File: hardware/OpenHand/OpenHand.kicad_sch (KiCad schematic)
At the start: 98 parts, among them J1 CONN_MOTOR_1, J10 CONN_JTAG, J11 CONN_FDBK_2, J12 CONN_EMG_2, J13 CONN_POS_3, J2 CONN_MOTOR_2, J3 CONN_BATT, J4 USB_C_CONN, J5 CONN_POS_1, J6 CONN_MOTOR_3, J7 CONN_FDBK_1, J8 CONN_EMG_1, J9 CONN_POS_2, Q1 2N7002, Q2 2N7002, SW1 SW_Push, SW2 BTN_RST, SW3 BTN_BOOT, U1 CH340C, U2 STM32F103RETx

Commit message: update schm and pcb again
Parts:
- removed JP9: JMPR_RST, Jumper:SolderJumper-2_P1.3mm_Bridged_RoundedPad1.0x1.5mm, symbol Jumper:SolderJumper_2_Bridged
- removed JP9: JMPR_BOOT, Jumper:SolderJumper-2_P1.3mm_Bridged_RoundedPad1.0x1.5mm, symbol Jumper:SolderJumper_2_Bridged
- removed TP50: TP_UC_BOOT, TestPoint:TestPoint_Pad_D1.0mm, symbol Connector:TestPoint_Small
- removed TP50: TP_UC_RST, TestPoint:TestPoint_Pad_D1.0mm, symbol Connector:TestPoint_Small
- added JP9: JMPR_RST, Jumper:SolderJumper-2_P1.3mm_Bridged_RoundedPad1.0x1.5mm, symbol Jumper:SolderJumper_2_Bridged
- added JP9: JMPR_BOOT, Jumper:SolderJumper-2_P1.3mm_Bridged_RoundedPad1.0x1.5mm, symbol Jumper:SolderJumper_2_Bridged
- added TP50: TP_UC_BOOT, TestPoint:TestPoint_Pad_D1.0mm, symbol Connector:TestPoint_Small
- added TP50: TP_UC_RST, TestPoint:TestPoint_Pad_D1.0mm, symbol Connector:TestPoint_Small
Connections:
- net UC_BOOT: now also C4.1, JP9.2 (B), TP50.1
- net UC_RST: now also C3.1, JP9.2 (B), TP50.1
- net at Q1.3 (D): now also JP9.1 (A); no longer C3.1
- net at Q2.3 (D): now also JP9.1 (A); no longer C4.1
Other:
- added sheet ESP32 (ESP32.kicad_sch)
- note added: "For now we have a parallel connection to this STM32, as well as ESP32 on another sheet, so we can later select which processor we will use, and can have two prototypes: one with ESP32 and one with STM32 MCU."

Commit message: Major updates to schm and pcb, a bit better design
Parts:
- removed J4: USB_C_CONN, Connector_USB:USB_C_Receptacle_G-Switch_GT-USB-7010ASV, symbol Connector:USB_C_Receptacle
- removed JP15, JP16, JP17, JP18: SolderJumper_2_Open, Jumper:SolderJumper-2_P1.3mm_Open_RoundedPad1.0x1.5mm, symbol Jumper:SolderJumper_2_Open
- removed JP9: JMPR_BTN_BOOT, Jumper:SolderJumper-2_P1.3mm_Bridged_RoundedPad1.0x1.5mm, symbol Jumper:SolderJumper_2_Bridged
- removed JP9: JMPR_BTN_RST, Jumper:SolderJumper-2_P1.3mm_Bridged_RoundedPad1.0x1.5mm, symbol Jumper:SolderJumper_2_Bridged
- removed JP9: JMPR_USB_P, Jumper:SolderJumper-2_P1.3mm_Bridged_RoundedPad1.0x1.5mm, symbol Jumper:SolderJumper_2_Bridged
- removed JP9: JMPR_RST, Jumper:SolderJumper-2_P1.3mm_Bridged_RoundedPad1.0x1.5mm, symbol Jumper:SolderJumper_2_Bridged
- removed JP9: JMPR_BOOT, Jumper:SolderJumper-2_P1.3mm_Bridged_RoundedPad1.0x1.5mm, symbol Jumper:SolderJumper_2_Bridged
- removed JP9: JMPR_TX, Jumper:SolderJumper-2_P1.3mm_Bridged_RoundedPad1.0x1.5mm, symbol Jumper:SolderJumper_2_Bridged
- removed JP9: JMPR_USB_N, Jumper:SolderJumper-2_P1.3mm_Bridged_RoundedPad1.0x1.5mm, symbol Jumper:SolderJumper_2_Bridged
- removed JP9: JMPR_RX, Jumper:SolderJumper-2_P1.3mm_Bridged_RoundedPad1.0x1.5mm, symbol Jumper:SolderJumper_2_Bridged
- removed Q1, Q2: 2N7002, Package_TO_SOT_SMD:SOT-23, symbol Transistor_FET:2N7002
- removed R10, R7, R8, R9: 10k, Resistor_SMD:R_0805_2012Metric_Pad1.20x1.40mm_HandSolder, symbol Device:R
- removed R4: 1k, Resistor_SMD:R_0805_2012Metric_Pad1.20x1.40mm_HandSolder, symbol Device:R
- removed SW3: BTN_BOOT, Button_Switch_SMD:SW_Tactile_SPST_NO_Straight_CK_PTS636Sx25SMTRLFS, symbol Switch:SW_Push
- removed TP50: TP_UC_PIN_PC15, TestPoint:TestPoint_Pad_D1.0mm, symbol Connector:TestPoint_Small
- removed TP50: TP_UC_BOOT, TestPoint:TestPoint_Pad_D1.0mm, symbol Connector:TestPoint_Small
- removed TP50: TP_UC_PIN_PC0, TestPoint:TestPoint_Pad_D1.0mm, symbol Connector:TestPoint_Small
- removed TP50: TP_UC_PIN_PC14, TestPoint:TestPoint_Pad_D1.0mm, symbol Connector:TestPoint_Small
- removed TP50: TP_USB_D_P, TestPoint:TestPoint_Pad_D1.0mm, symbol Connector:TestPoint_Small
- removed TP50: TP_HW_REV_1, TestPoint:TestPoint_Pad_D1.0mm, symbol Connector:TestPoint_Small
- removed TP50: TP_UC_PIN_PC3, TestPoint:TestPoint_Pad_D1.0mm, symbol Connector:TestPoint_Small
- removed TP50: TP_UC_PIN_PD2, TestPoint:TestPoint_Pad_D1.0mm, symbol Connector:TestPoint_Small
- removed TP50: TP_UC_SCL, TestPoint:TestPoint_Pad_D1.0mm, symbol Connector:TestPoint_Small
- removed TP50: TP_HW_REV_2, TestPoint:TestPoint_Pad_D1.0mm, symbol Connector:TestPoint_Small
- removed TP50: TP_UC_PIN_PB10, TestPoint:TestPoint_Pad_D1.0mm, symbol Connector:TestPoint_Small
- removed TP50: TP_UC_PIN_PD0, TestPoint:TestPoint_Pad_D1.0mm, symbol Connector:TestPoint_Small
- removed TP50: TP_UC_SDA, TestPoint:TestPoint_Pad_D1.0mm, symbol Connector:TestPoint_Small
- removed TP50: TP_UC_PIN_PB11, TestPoint:TestPoint_Pad_D1.0mm, symbol Connector:TestPoint_Small
- removed TP50: TP_LED_2, TestPoint:TestPoint_Pad_D1.0mm, symbol Connector:TestPoint_Small
- removed TP50: TP_UC_RST, TestPoint:TestPoint_Pad_D1.0mm, symbol Connector:TestPoint_Small
- removed TP50: TP_UC_PIN_PC13, TestPoint:TestPoint_Pad_D1.0mm, symbol Connector:TestPoint_Small
- removed TP50: TP_UC_PIN_PD1, TestPoint:TestPoint_Pad_D1.0mm, symbol Connector:TestPoint_Small
- removed TP50: TP_UC_PIN_PC1, TestPoint:TestPoint_Pad_D1.0mm, symbol Connector:TestPoint_Small
- removed TP50: TP_LED_1, TestPoint:TestPoint_Pad_D1.0mm, symbol Connector:TestPoint_Small
- removed TP50: TP_UC_PIN_PC2, TestPoint:TestPoint_Pad_D1.0mm, symbol Connector:TestPoint_Small
- removed TP50: TP_HW_REV_3, TestPoint:TestPoint_Pad_D1.0mm, symbol Connector:TestPoint_Small
- removed TP50: TP_UC_PIN_PB2, TestPoint:TestPoint_Pad_D1.0mm, symbol Connector:TestPoint_Small
- removed TP50: TP_HW_REV_4, TestPoint:TestPoint_Pad_D1.0mm, symbol Connector:TestPoint_Small
- removed U1: CH340C, Package_SO:SOIC-16_3.9x9.9mm_P1.27mm, symbol Interface_USB:CH340C
- added C5, C6: 100n, Capacitor_SMD:C_0805_2012Metric, symbol Device:C
- added J5: USB_C_CONN, Connector_USB:USB_C_Receptacle_G-Switch_GT-USB-7010ASV, symbol Connector:USB_C_Receptacle_USB2.0
- added JP14, JP7, JP8, JP9: SolderJumper_2_Open, Jumper:SolderJumper-2_P1.3mm_Open_RoundedPad1.0x1.5mm, symbol Jumper:SolderJumper_2_Open
- added R13, R16, R5, R55: 10k, Resistor_SMD:R_0805_2012Metric, symbol Device:R
- added R52: 1.5k, Resistor_SMD:R_0805_2012Metric, symbol Device:R
- added R54: 47k, Resistor_SMD:R_0805_2012Metric, symbol Device:R
- added SW1: BTN_RST, Button_Switch_SMD:SW_Tactile_SPST_NO_Straight_CK_PTS636Sx25SMTRLFS, symbol Switch:SW_Push
- added TP50: TP_UC_PIN_PD2, TestPoint:TestPoint_Pad_D1.0mm, symbol Connector:TestPoint_Small
- added TP50: TP_BATT_SENSE, TestPoint:TestPoint_Pad_D1.0mm, symbol Connector:TestPoint_Small
- added TP50: TP_UC_PIN_PC12, TestPoint:TestPoint_Pad_D1.0mm, symbol Connector:TestPoint_Small
- added TP50: TP_HALL_03, TestPoint:TestPoint_Pad_D1.0mm, symbol Connector:TestPoint_Small
- added TP50: TP_UC_SCL, TestPoint:TestPoint_Pad_D1.0mm, symbol Connector:TestPoint_Small
- added TP50: TP_UC_SDA, TestPoint:TestPoint_Pad_D1.0mm, symbol Connector:TestPoint_Small
- added TP50: TP_BTN_RST, TestPoint:TestPoint_Pad_D1.0mm, symbol Connector:TestPoint_Small
- added TP50: TP_BTN_BOOT, TestPoint:TestPoint_Pad_D1.0mm, symbol Connector:TestPoint_Small
- added TP50: TP_USB_D_P, TestPoint:TestPoint_Pad_D1.0mm, symbol Connector:TestPoint_Small
- added TP50: TP_UC_PIN_PA6, TestPoint:TestPoint_Pad_D1.0mm, symbol Connector:TestPoint_Small
- added TP50: TP_UC_PIN_PA5, TestPoint:TestPoint_Pad_D1.0mm, symbol Connector:TestPoint_Small
- added TP50: TP_HALL_01, TestPoint:TestPoint_Pad_D1.0mm, symbol Connector:TestPoint_Small
- added TP50: TP_UC_PIN_PD1, TestPoint:TestPoint_Pad_D1.0mm, symbol Connector:TestPoint_Small
- added TP50: TP_HALL_02, TestPoint:TestPoint_Pad_D1.0mm, symbol Connector:TestPoint_Small
- C1: value 1u -> 100n; footprint Capacitor_SMD:C_1206_3216Metric_Pad1.33x1.80mm_HandSolder -> Capacitor_SMD:C_0805_2012Metric
- C2, C3, C4: footprint Capacitor_SMD:C_1206_3216Metric_Pad1.33x1.80mm_HandSolder -> Capacitor_SMD:C_0805_2012Metric
- D1, D2: footprint LED_SMD:LED_0805_2012Metric -> LED_SMD:LED_1210_3225Metric
- R1: value 5k1 -> 10k; footprint Resistor_SMD:R_0805_2012Metric_Pad1.20x1.40mm_HandSolder -> Resistor_SMD:R_0805_2012Metric
- R10: renamed from R13; footprint Resistor_SMD:R_0805_2012Metric_Pad1.20x1.40mm_HandSolder -> Resistor_SMD:R_0805_2012Metric
- R14, R15, R2, R51, R52: footprint Resistor_SMD:R_0805_2012Metric_Pad1.20x1.40mm_HandSolder -> Resistor_SMD:R_0805_2012Metric
- R3: value 1k -> 5k1; footprint Resistor_SMD:R_0805_2012Metric_Pad1.20x1.40mm_HandSolder -> Resistor_SMD:R_0805_2012Metric
- R8: renamed from R12; footprint Resistor_SMD:R_0805_2012Metric_Pad1.20x1.40mm_HandSolder -> Resistor_SMD:R_0805_2012Metric
- R9: renamed from R11; footprint Resistor_SMD:R_0805_2012Metric_Pad1.20x1.40mm_HandSolder -> Resistor_SMD:R_0805_2012Metric
- SW2: value BTN_RST -> BTN_BOOT
- TP50: value TP_UC_PIN_PB5 -> TP_UC_PIN_PB12
- renumbered J5 to J4, RV2 to RV1, RV3 to RV2, RV1 to RV3, SW1 to SW3, U2 to U1
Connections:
- net MOTOR_1_EN is gone; now on an unnamed net: U1.33 (PB12)
- net MOTOR_3_UC2 is gone; now on net UC_TX: U1.51 (PC10)
- net TRIM_POT_1 is gone; now on net TRIM_POT_01: JP9.2 (B)
- net TRIM_POT_2 is gone; now on net TRIM_POT_02: JP9.2 (B)
- net TRIM_POT_3 is gone; now on net TRIM_POT_03: JP9.2 (B)
- net USB_D_N is gone; now on net USB_D-: TP34.1
- net +3V3: now also C3.1, C4.1, R1.1, C5.1, C6.1, R13.1, R16.1, R5.1, R52.2
- net +5V: now also J5.A4 (VBUS), J5.A9 (VBUS), J5.B4 (VBUS), J5.B9 (VBUS); no longer C1.1
- net Earth: now also JP11.1 (A), JP12.1 (A), JP13.1 (A), R3.2, C5.2, C6.2, J5.A1 (GND), J5.A12 (GND), J5.B1 (GND), J5.B12 (GND), JP14.1 (A), R55.1, SW1.2; no longer R1.2
- net HALL_SENS_01_S: now also U1.9 (PC1), TP50.1
- net HALL_SENS_02_S: now also U1.10 (PC2), TP50.1
- net HALL_SENS_03_S: now also U1.11 (PC3), TP50.1
- net LED_1: now also U1.57 (PB5); no longer U1.52 (PC11)
- net LED_2: now also U1.58 (PB6); no longer U1.53 (PC12)
- net UC_BOOT: now also C2.1, SW2.1, R5.2, TP50.1; no longer C4.1
- net UC_RST: now also C1.1, R1.2, SW1.1, TP50.1; no longer C3.1
- net UC_RX: now also U1.52 (PC11); no longer U1.59 (PB7)
- net UC_SCL: now also TP50.1
- net UC_SDA: now also TP50.1
- net UC_TX: no longer U1.58 (PB6)
- net HW_REV_03: now reaches U1.4 (PC15)
- net HW_REV_03: now also JP13.2 (B), JP9.1 (A)
- net at R15.2: now also JP9.2 (B)
- net HW_REV_01: now reaches JP11.2 (B)
- net HW_REV_01: now also U1.2 (PC13), JP7.1 (A)
- net at JP10.2 (B): now also R16.2
- net at U1.8 (PC0): now also R54.1, R55.2, TP50.1
- net at R14.2: now also JP8.2 (B); no longer SW2.1
- net at R2.1: now also J5.A5 (CC1)
- net HW_REV_02: now reaches U1.3 (PC14)
- net HW_REV_02: now also JP12.2 (B), JP8.1 (A)
- net at R3.1: now also J5.B5 (CC2)
- net at U1.54 (PD2): now also TP50.1
- net at TP50.1: no longer U1.57 (PB5)
- net MOTOR_03_FAULT: now reaches U1.29 (PB10)
- net HW_REV_04: now reaches U1.5 (PD0)
- net HW_REV_04: now also JP10.1 (A), JP14.2 (B)
- net HAPTIC_FAULT: now reaches U1.30 (PB11)
- net MOTOR_02_FAULT: now reaches U1.28 (PB2)
- net at U1.6 (PD1): now also TP50.1
- net ADC_1_ALERT_RDY renamed MOTOR_02_EN
- net ADC_2_ALERT_RDY renamed MOTOR_03_EN
- net BTN_1 renamed BTN_01
- net BTN_01: now also U1.59 (PB7)
- net EMG_1_N renamed EMG_01_P
- net EMG_1_P renamed EMG_01_N
- net EMG_1_UC renamed HAPTIC_EN
- net EMG_2_N renamed EMG_02_P
- net EMG_2_P renamed EMG_02_N
- net EMG_2_UC renamed MOTOR_01_FAULT
- net FDBK_MOTOR_1_N renamed HAPTIC_01_N
- net FDBK_MOTOR_1_P renamed HAPTIC_01_P
- net FDBK_MOTOR_1_UC1 renamed HAPTIC_01_PWM
- net FDBK_MOTOR_1_UC2 renamed MOTOR_03_PWM
- net FDBK_MOTOR_2_N renamed HAPTIC_02_N
- net FDBK_MOTOR_2_P renamed HAPTIC_02_P
- net FDBK_MOTOR_2_UC1 renamed MOTOR_03_DIR
- net FDBK_MOTOR_2_UC2 renamed MOTOR_02_DIR
- net FDBK_MOTOR_EN renamed HAPTIC_01_DIR
- net FDBK_MOTOR_FAULT renamed MOTOR_01_EN
- net HW_REV_1 renamed TRIM_POT_01
- net TRIM_POT_01: no longer JP10.1 (A)
- net HW_REV_2 renamed TRIM_POT_02
- net TRIM_POT_02: no longer JP11.1 (A)
- net HW_REV_3 renamed TRIM_POT_03
- net TRIM_POT_03: no longer JP12.1 (A)
- net HW_REV_4 renamed EMG_01_UC
- net EMG_01_UC: no longer JP13.1 (A)
- net MOTOR_1_FAULT renamed EMG_02_UC
- net MOTOR_1_N renamed MOTOR_01_N
- net MOTOR_1_P renamed MOTOR_01_P
- net MOTOR_1_UC1 renamed MOTOR_02_PWM
- net MOTOR_1_UC2 renamed USB_D-
- net USB_D-: now also J5.A6 (D+), J5.B6 (D+)
- net MOTOR_2_EN renamed HAPTIC_02_DIR
- net MOTOR_2_FAULT: no longer names the net of U1.21 (PA5)
- net MOTOR_2_FAULT: now also TP50.1
- net MOTOR_2_N renamed MOTOR_02_N
- net MOTOR_2_P renamed MOTOR_02_P
- net MOTOR_2_UC1 renamed MOTOR_01_DIR
- net MOTOR_2_UC2 renamed USB_D+
- net USB_D+: now also J5.A7 (D-), J5.B7 (D-), R52.1, TP50.1
- net MOTOR_3_EN renamed HAPTIC_02_PWM
- net MOTOR_3_FAULT: no longer names the net of U1.22 (PA6)
- net MOTOR_3_FAULT: now also TP50.1
- net MOTOR_3_N renamed MOTOR_03_N
- net MOTOR_3_P renamed MOTOR_03_P
- net MOTOR_3_UC1 renamed MOTOR_01_PWM
- new net: TP50.1, U1.53 (PC12)
- new net: JP7.2 (B), R13.2
- new net +BATT: R54.2
- no-connect marks 15 -> 3
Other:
- sheet Control, Analog renamed Motor Control
- removed sheet ESP32
- sheet Motor Control: file Control.kicad_sch -> MotorControl.kicad_sch
- note added: "ADC inputs"
- note added: "Battery voltage sense divider: - max bat voltage ~12.6V - gives us ~2.2V on output"
- note added: "Buttons for RST and BOOT"
- note added: "Direct USB device connection"
- note added: "EMG ADC inputs"
- note added: "HW REV"
- note added: "I2C pullups"
- note added: "JTAG debugging"
- note added: "Just in case I2C"
- note added: "Just in case UART"
- note added: "STM32 decoupling caps"
- note removed: "For now we have a parallel connection to this STM32, as well as ESP32 on another sheet, so we can later select which processor we will use, and can have two prototypes: one with ESP32 and one with STM32 MCU."
- note removed: "I2C pullups and test points"
- note removed: "UART test points"
- note removed: "USB to UART converter for debugging"
- moved on the sheet: D1, D2, JP9, R10, R51, R52, R8, R9, RV1, RV2, RV3, SW3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

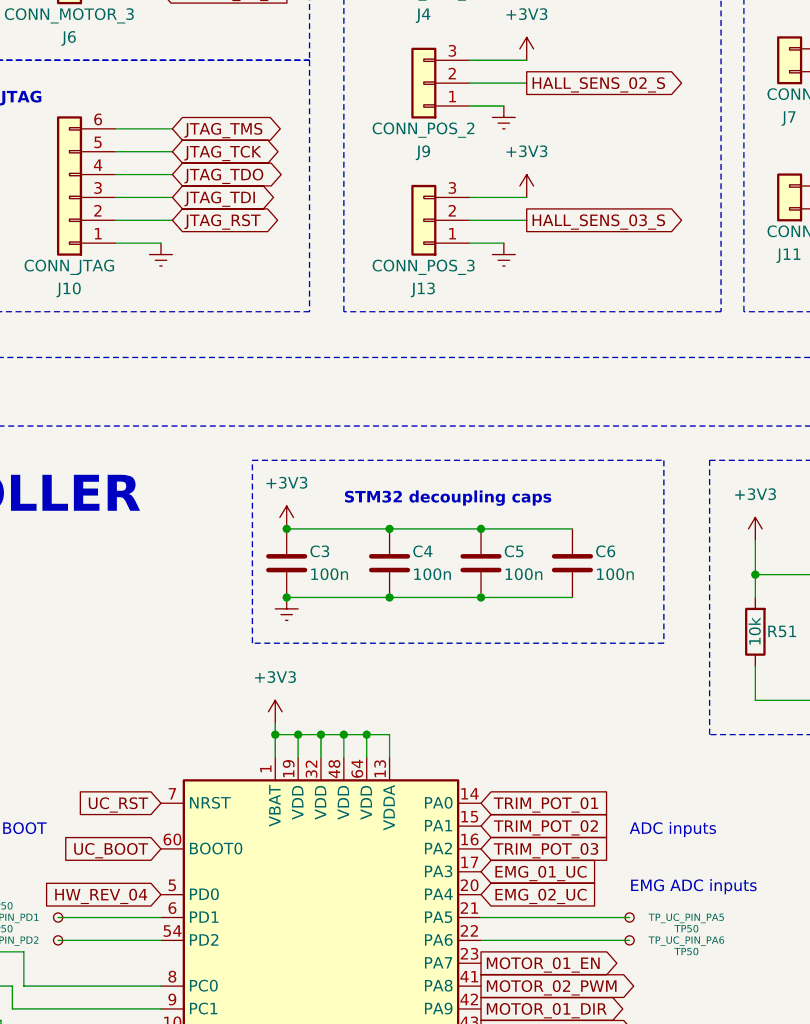
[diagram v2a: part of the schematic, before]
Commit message: Update PCB design/layout
Still WIP, routing traces currently
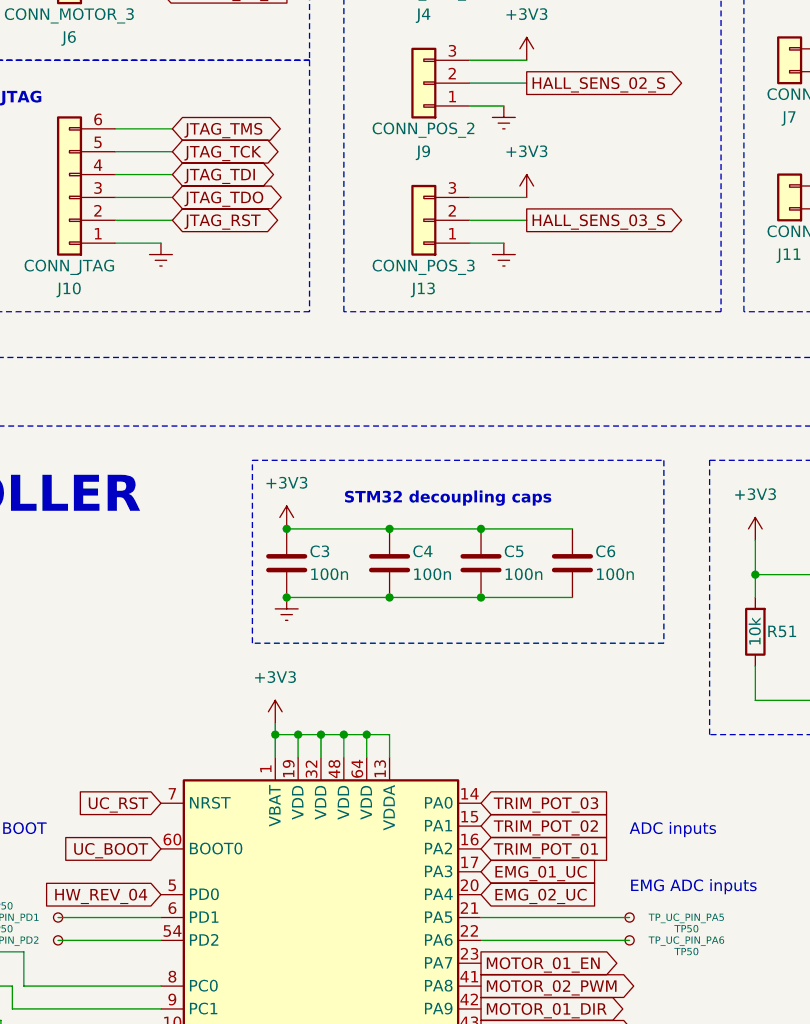
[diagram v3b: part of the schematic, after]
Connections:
- net JTAG_TDI: now also J10.4 (Pin_4); no longer J10.3 (Pin_3)
- net JTAG_TDO: now also J10.3 (Pin_3); no longer J10.4 (Pin_4)
- net TRIM_POT_01: now also U1.16 (PA2); no longer U1.14 (PA0)
- net TRIM_POT_03: now also U1.14 (PA0); no longer U1.16 (PA2)
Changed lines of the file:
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@@
+    (stroke (width 0) (type default))
+  )
+  (wire (pts (xy 81.28 91.44) (xy 87.63 91.44))
     (stroke (width 0) (type default))
   )
@@
     (stroke (width 0) (type default))
   )
-  (wire (pts (xy 81.28 91.44) (xy 87.63 91.44))
-    (stroke (width 0) (type default))
-  )
   (wire (pts (xy 152.4 147.32) (xy 171.45 147.32))
     (stroke (width 0) (type default))
@@
     (stroke (width 0) (type default))
   )
+  (wire (pts (xy 81.28 88.9) (xy 87.63 88.9))
+    (stroke (width 0) (type default))
+  )
   (wire (pts (xy 120.65 60.96) (xy 127 60.96))
     (stroke (width 0) (type default))
@@
   )
   (wire (pts (xy 254 59.69) (xy 254 58.42))
-    (stroke (width 0) (type default))
-  )
-  (wire (pts (xy 81.28 88.9) (xy 87.63 88.9))
     (stroke (width 0) (type default))
   )
@@
     )
   )
+  (global_label "TRIM_POT_03" (shape input) (at 121.92 158.75 0) (fields_autoplaced)
+    (effects (font (size 1.27 1.27)) (justify left))
+    (property "Intersheetrefs" "${INTERSHEET_REFS}" (at 137.1213 158.75 0)
+      (effects (font (size 1.27 1.27)) (justify left) hide)
+    )
+  )
   (global_label "HALL_SENS_01_S" (shape input) (at 58.42 179.07 180) (fields_autoplaced)
     (effects (font (size 1.27 1.27)) (justify right))
@@
     )
   )
-  (global_label "JTAG_TDO" (shape bidirectional) (at 87.63 88.9 0) (fields_autoplaced)
-    (effects (font (size 1.27 1.27)) (justify left))
-    (property "Intersheetrefs" "${INTERSHEET_REFS}" (at 100.556 88.9 0)
+  (global_label "JTAG_TDO" (shape bidirectional) (at 87.63 91.44 0) (fields_autoplaced)
+    (effects (font (size 1.27 1.27)) (justify left))
+    (property "Intersheetrefs" "${INTERSHEET_REFS}" (at 100.556 91.44 0)
       (effects (font (size 1.27 1.27)) (justify left) hide)
     )
@@
     )
   )
-  (global_label "TRIM_POT_01" (shape input) (at 121.92 158.75 0) (fields_autoplaced)
-    (effects (font (size 1.27 1.27)) (justify left))
-    (property "Intersheetrefs" "${INTERSHEET_REFS}" (at 137.1213 158.75 0)
-      (effects (font (size 1.27 1.27)) (justify left) hide)
-    )
-  )
   (global_label "HAPTIC_01_P" (shape input) (at 163.83 74.93 0) (fields_autoplaced)
     (effects (font (size 1.27 1.27)) (justify left))
@@
     )
   )
-  (global_label "TRIM_POT_03" (shape input) (at 121.92 163.83 0) (fields_autoplaced)
+  (global_label "UC_BOOT" (shape input) (at 86.36 163.83 180) (fields_autoplaced)
+    (effects (font (size 1.27 1.27)) (justify right))
+    (property "Intersheetrefs" "${INTERSHEET_REFS}" (at 74.9081 163.83 0)
+      (effects (font (size 1.27 1.27)) (justify right) hide)
+    )
+  )
+  (global_label "TRIM_POT_01" (shape input) (at 121.92 163.83 0) (fields_autoplaced)
     (effects (font (size 1.27 1.27)) (justify left))
     (property "Intersheetrefs" "${INTERSHEET_REFS}" (at 137.1213 163.83 0)
@@
     )
   )
-  (global_label "UC_BOOT" (shape input) (at 86.36 163.83 180) (fields_autoplaced)
-    (effects (font (size 1.27 1.27)) (justify right))
-    (property "Intersheetrefs" "${INTERSHEET_REFS}" (at 74.9081 163.83 0)
-      (effects (font (size 1.27 1.27)) (justify right) hide)
-    )
-  )
   (global_label "LED_2" (shape input) (at 215.9 154.94 180) (fields_autoplaced)
     (effects (font (size 1.27 1.27)) (justify right))
@@
     )
   )
-  (global_label "JTAG_TDI" (shape bidirectional) (at 87.63 91.44 0) (fields_autoplaced)
-    (effects (font (size 1.27 1.27)) (justify left))
-    (property "Intersheetrefs" "${INTERSHEET_REFS}" (at 99.8303 91.44 0)
-      (effects (font (size 1.27 1.27)) (justify left) hide)
-    )
+  (global_label "JTAG_TDI" (shape bidirectional) (at 87.63 88.9 0) (fields_autoplaced)
+    (effects (font (size 1.27 1.27)) (justify left))
+    (property "Intersheetrefs" "${INTERSHEET_REFS}" (at 99.8303 88.9 0)
+      (effects (font (size 1.27 1.27)) (justify left) hide)
+    )
